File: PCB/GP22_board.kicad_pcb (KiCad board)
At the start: 4 copper layers, 100 x 100 mm, 146 parts, among them CON1 5V power input, IC1 ATMEGA328P-A, P1 TTLOut1, P10 S- DC/AC, P11 S+ DC/AC, P12 S- DC/AC, P13 TTLOut2, P14 TTLOut3, P15 PWR_SEL, P16 FILT_SEL, P2 SineInput, P3 TTLInput, P4 USB_OTG, P5 ICSP, P6 STInput, P7 S+ DC/AC, P8 S- DC/AC, P9 S+ DC/AC, SW1 START, SW2 STOP1, SW3 STOP2, U1 RS 252-210, U10 XC6206, U11 ISO7242, U12 FT232RL, U2 GP22, U3 LTC6957-4, U4 ISO3088, U5 IDT49FCT, U6 LD1117S33TR, U7 MC74VHC1GT04, U8 SN74LV8154, U9 SC74HC165N, X1 TSX-3225 X1E0000210013, Y1 4MHz, Y2 32.768 kHz

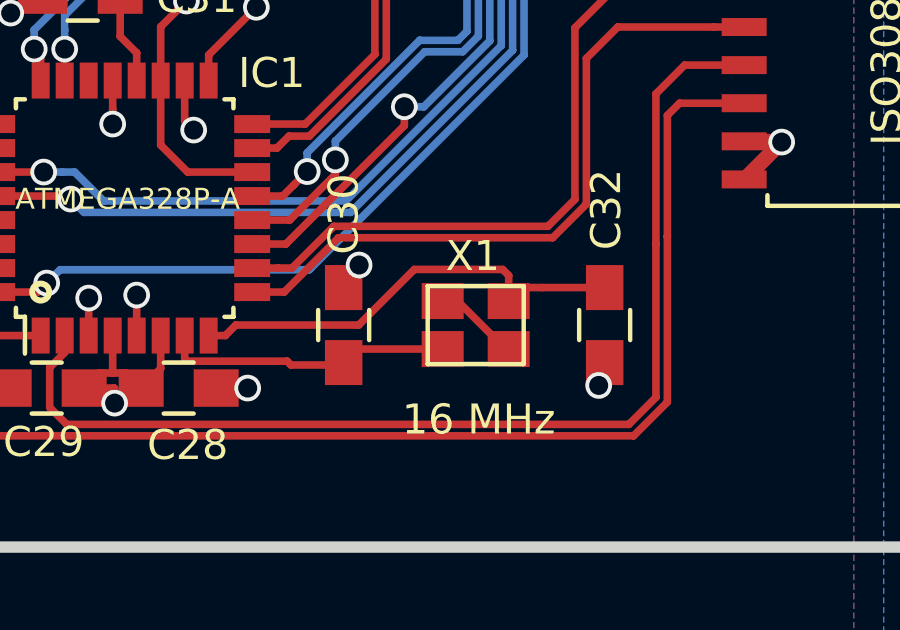
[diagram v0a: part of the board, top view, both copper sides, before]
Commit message: Create netlist and update board: no changes except to crystal grounding
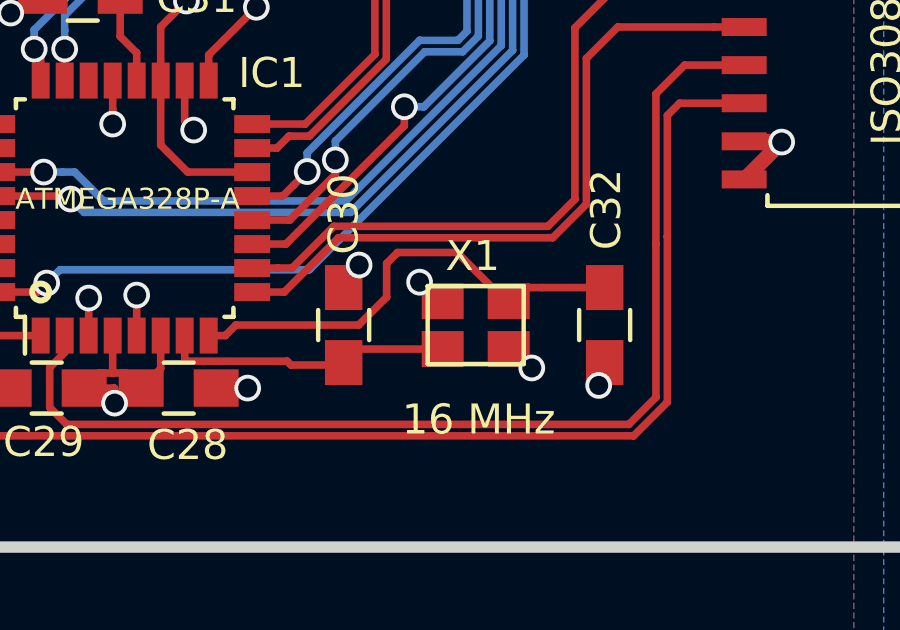
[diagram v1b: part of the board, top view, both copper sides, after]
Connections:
- D1 pad 1: (no net) -> Net-(D1-Pad1)
- D1 pad 5: (no net) -> Net-(D1-Pad5)
- D6 pad 1: (no net) -> Net-(D6-Pad1)
- D6 pad 5: (no net) -> Net-(D6-Pad5)
- D7 pad 1: (no net) -> Net-(D7-Pad1)
- D7 pad 5: (no net) -> Net-(D7-Pad5)
- IC1 pad 22: (no net) -> /DIYino/A7_inputonly
- JP1 pad 1: (no net) -> Net-(JP1-Pad1)
- P4 pad 4: (no net) -> Net-(P4-Pad4)
- SW1 pad 2a: (no net) -> Net-(SW1-Pad2a)
- SW1 pad 3a: (no net) -> Net-(SW1-Pad3a)
- SW1 pad 3b: (no net) -> Net-(SW1-Pad3b)
- SW2 pad 2a: (no net) -> Net-(SW2-Pad2a)
- SW2 pad 3a: (no net) -> Net-(SW2-Pad3a)
- SW2 pad 3b: (no net) -> Net-(SW2-Pad3b)
- SW3 pad 2a: (no net) -> Net-(SW3-Pad2a)
- SW3 pad 3a: (no net) -> Net-(SW3-Pad3a)
- SW3 pad 3b: (no net) -> Net-(SW3-Pad3b)
- U1 pad A17: (no net) -> Net-(U1-PadA17)
- U1 pad A18: (no net) -> Net-(U1-PadA18)
- U1 pad A19: (no net) -> Net-(U1-PadA19)
- U1 pad A20: (no net) -> Net-(U1-PadA20)
- U1 pad A21: (no net) -> /BPSubsheet/21A
- U1 pad A22: (no net) -> /BPSubsheet/22A
- U1 pad A23: (no net) -> /BPSubsheet/23A
- U1 pad A24: (no net) -> /BPSubsheet/24A
- U1 pad A25: (no net) -> /BPSubsheet/25A
- U1 pad A26: (no net) -> /BPSubsheet/26A
- U1 pad A27: (no net) -> /BPSubsheet/27A
- U1 pad A28: (no net) -> /BPSubsheet/28A
- U1 pad A29: (no net) -> /BPSubsheet/29A
- U1 pad A30: (no net) -> /BPSubsheet/30A
- U1 pad B17: (no net) -> Net-(U1-PadB17)
- U1 pad B18: (no net) -> Net-(U1-PadB18)
- U1 pad B19: (no net) -> Net-(U1-PadB19)
- U1 pad B20: (no net) -> Net-(U1-PadB20)
- U1 pad B21: (no net) -> /BPSubsheet/21B
- U1 pad B22: (no net) -> /BPSubsheet/22B
- U1 pad B23: (no net) -> /BPSubsheet/23B
- U1 pad B24: (no net) -> /BPSubsheet/24B
- U1 pad B25: (no net) -> /BPSubsheet/25B
- U1 pad B26: (no net) -> /BPSubsheet/26B
- U1 pad B27: (no net) -> /BPSubsheet/27B
- U1 pad B28: (no net) -> /BPSubsheet/28B
- U1 pad B29: (no net) -> /BPSubsheet/29B
- U1 pad B30: (no net) -> /BPSubsheet/30B
- U1 pad C17: (no net) -> Net-(U1-PadC17)
- U1 pad C18: (no net) -> Net-(U1-PadC18)
- U1 pad C19: (no net) -> Net-(U1-PadC19)
- U1 pad C20: (no net) -> Net-(U1-PadC20)
- U1 pad C21: (no net) -> /BPSubsheet/21C
- U1 pad C22: (no net) -> /BPSubsheet/22C
- U1 pad C23: (no net) -> /BPSubsheet/23C
- U1 pad C24: (no net) -> /BPSubsheet/24C
- U1 pad C25: (no net) -> /BPSubsheet/25C
- U1 pad C26: (no net) -> /BPSubsheet/26C
- U1 pad C27: (no net) -> /BPSubsheet/27C
- U1 pad C28: (no net) -> /BPSubsheet/28C
- U1 pad C29: (no net) -> /BPSubsheet/29C
- U1 pad C30: (no net) -> /BPSubsheet/30C
- U11 pad 10: (no net) -> Net-(U11-Pad10)
- U11 pad 11: (no net) -> Net-(U11-Pad11)
- U11 pad 6: (no net) -> /DIYino/ISO_OUTPUT
- U11 pad 7: (no net) -> Net-(U11-Pad7)
- U12 pad 10: (no net) -> Net-(U12-Pad10)
- U12 pad 11: (no net) -> Net-(U12-Pad11)
- U12 pad 12: (no net) -> Net-(U12-Pad12)
- U12 pad 13: (no net) -> Net-(U12-Pad13)
- U12 pad 14: (no net) -> Net-(U12-Pad14)
- U12 pad 19: (no net) -> Net-(U12-Pad19)
- U12 pad 24: (no net) -> Net-(U12-Pad24)
- U12 pad 27: (no net) -> Net-(U12-Pad27)
- U12 pad 28: (no net) -> Net-(U12-Pad28)
- U12 pad 3: (no net) -> Net-(U12-Pad3)
- U12 pad 6: (no net) -> Net-(U12-Pad6)
- U12 pad 8: (no net) -> Net-(U12-Pad8)
- U12 pad 9: (no net) -> Net-(U12-Pad9)
- U2 pad 17: (no net) -> Net-(U2-Pad17)
- U2 pad 18: (no net) -> Net-(U2-Pad18)
- U2 pad 19: (no net) -> Net-(U2-Pad19)
- U2 pad 20: (no net) -> Net-(U2-Pad20)
- U2 pad 23: (no net) -> Net-(U2-Pad23)
- U2 pad 24: (no net) -> Net-(U2-Pad24)
- U2 pad 5: (no net) -> /GP22_FIRE_UP
- U2 pad 6: (no net) -> /GP22_FIRE_DOWN
- U2 pad 7: (no net) -> /GP22_FIRE_IN
- U3 pad 10: (no net) -> Net-(U3-Pad10)
- U4 pad 11: (no net) -> Net-(U4-Pad11)
- U4 pad 14: (no net) -> Net-(U4-Pad14)
- U5 pad 11: (no net) -> Net-(U5-Pad11)
- U5 pad 13: (no net) -> Net-(U5-Pad13)
- U5 pad 14: (no net) -> Net-(U5-Pad14)
- U5 pad 15: (no net) -> Net-(U5-Pad15)
- U5 pad 17: (no net) -> Net-(U5-Pad17)
- U5 pad 18: (no net) -> Net-(U5-Pad18)
- U5 pad 19: (no net) -> Net-(U5-Pad19)
- U8 pad 8: (no net) -> Net-(U8-Pad8)
- U9 pad 7: (no net) -> Net-(U9-Pad7)
- X1 pad 3: Net-(X1-Pad3) -> GND
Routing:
- net GND: track 132.8 -> 135.7 mm, vias 60 -> 62
- net Net-(X1-Pad3): track 2.86 -> 0.00 mm
- net Net-(C32-Pad1): track 15.5 -> 16.1 mm

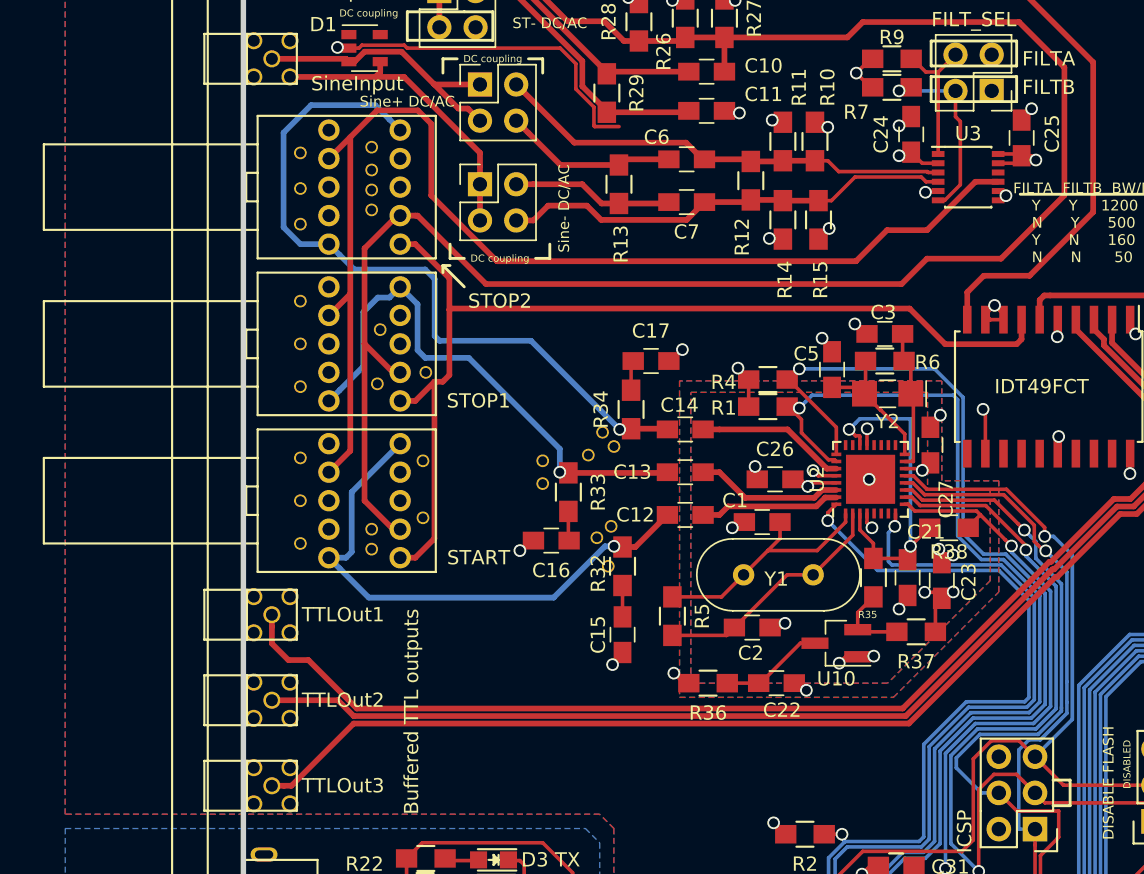
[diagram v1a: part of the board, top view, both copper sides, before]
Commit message: Fix Rotary switch footprint (NEVER TRUST KICAD FOOTPRINTS!!!)
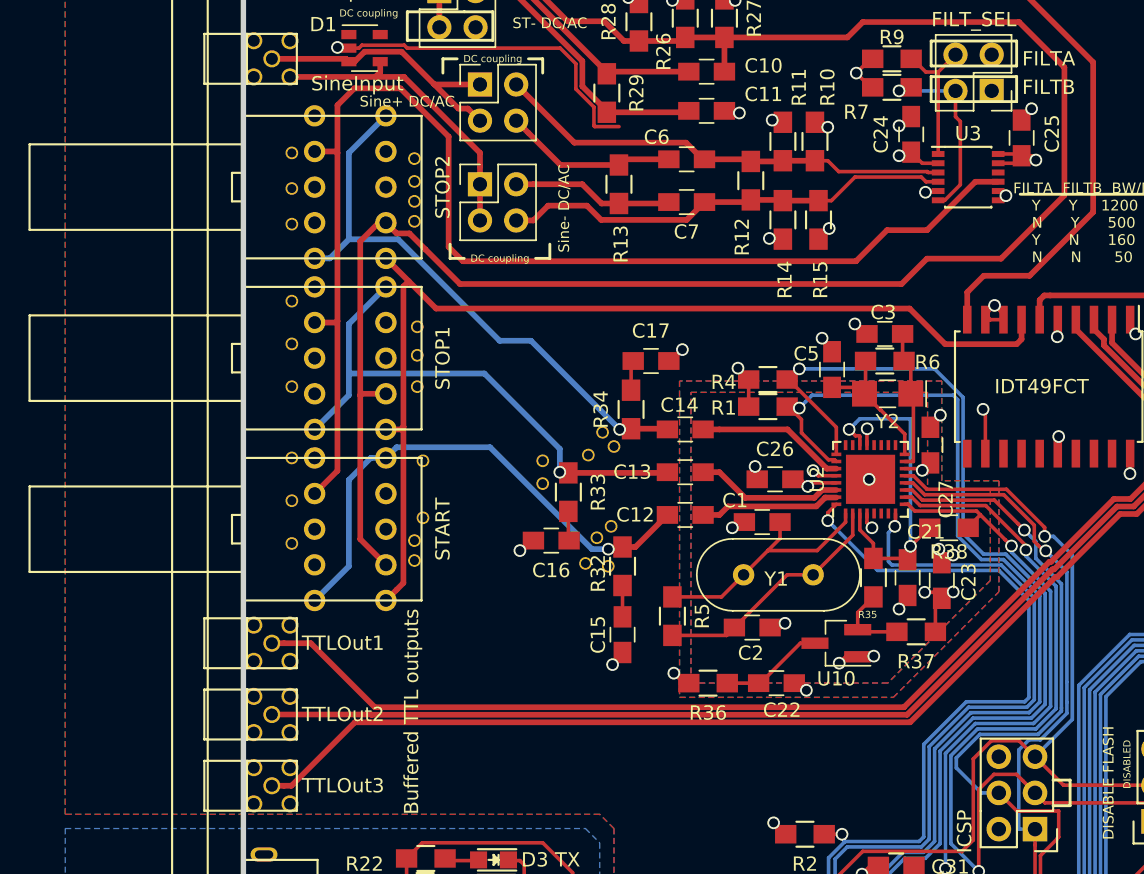
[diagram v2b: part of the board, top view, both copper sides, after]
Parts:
- added VIA**: ViaHack, Custom:ViaHack, F.Cu at (189.0, 95.4)
- SW1, SW2, SW3: footprint Custom:SP3T_switch -> Custom:ALPS_Rotary_SRBM
- moved SW1 11.2 mm to (165.0, 93.0)
- moved SW2 11.0 mm to (165.0, 81.0)
- moved SW3 11.0 mm to (165.0, 69.0)
- moved VIA** 3.10 mm to (177.0, 71.4)
- moved VIA** 3.10 mm to (177.0, 70.0)
- moved VIA** 3.10 mm to (177.0, 68.6)
- moved VIA** 3.10 mm to (177.0, 67.0)
- moved VIA** 3.10 mm to (177.0, 93.8)
- moved VIA** 3.10 mm to (177.0, 95.2)
- moved VIA** 2.81 mm to (177.2, 83.0)
- moved VIA** 2.61 mm to (177.2, 78.8)
- moved P1 2.00 mm to (167.0, 101.0)
- moved VIA** 1.34 mm to (177.2, 80.8)
- moved P13 1.00 mm to (167.0, 106.0)
- moved VIA** 0.60 mm to (168.4, 88.0)
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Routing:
- net /GP22_STOP2: track 51.5 -> 40.6 mm
- net /SineRectified: track 84.2 -> 89.9 mm
- net /TTLBufferedOut1: track 85.4 -> 83.3 mm
- net /GP22_START: track 38.1 -> 36.7 mm
- net /TTLBuffered: track 72.1 -> 73.0 mm
- net /GP22_STOP1: track 37.6 -> 38.3 mm

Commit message: Produce BOM with "Boms away"
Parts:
- removed JP1: DISABLE FLASH, Pin_Headers:Pin_Header_Straight_1x03
- removed P5: ICSP, Pin_Headers:Pin_Header_Straight_2x03
- added DISABLE_FLASH1: JMP, Pin_Headers:Pin_Header_Straight_1x03_Pitch2.54mm, F.Cu at (229.0, 113.5)
- added ICSP1: HEADER, Pin_Headers:Pin_Header_Straight_2x03_Pitch2.54mm, F.Cu at (220.5, 114.0)
- D1: footprint TO_SOT_Packages_SMD:SOT-23-5 -> TO_SOT_Packages_SMD:SOT-23-5_HandSoldering
- FILT_SEL1: renamed from P16; value FILT_SEL -> HEADER
- P10, P12, P8: value S- DC/AC -> HEADER
- P11, P7, P9: value S+ DC/AC -> HEADER
- POWER1: renamed from D2; value POWER -> LED
- POWER_SEL1: renamed from P15; value PWR_SEL -> JMP
- R12, R13, R18, R19, R28, R29: value R -> 50
- RX1: renamed from D4; value RX -> LED
- SCLK1: renamed from D5; value SCLK -> LED
- START1: renamed from SW1; value START -> DP3T
- STInput1: renamed from P6; value STInput -> MMCX
- STOP1: renamed from SW2; value STOP1 -> DP3T
- STOP2: renamed from SW3; value STOP2 -> DP3T
- SineInput1: renamed from P2; value SineInput -> MMCX
- TTLInput1: renamed from P3; value TTLInput -> MMCX
- TTLOut1: renamed from P1; value TTLOut1 -> MMCX
- TTLOut2: renamed from P13; value TTLOut2 -> MMCX
- TTLOut3: renamed from P14; value TTLOut3 -> MMCX
- TX1: renamed from D3; value TX -> LED
- U1: value RS 252-210 -> Right Angle
- U7: value MC74VHC1GT04 -> MC74VHC1G04DTT1G
- X1: value TSX-3225 X1E0000210013 -> TSX-3225 X1E0000210013

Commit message: Labelling tweaks
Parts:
- R12, R13, R18, R19, R28, R29: value 50 -> 50R

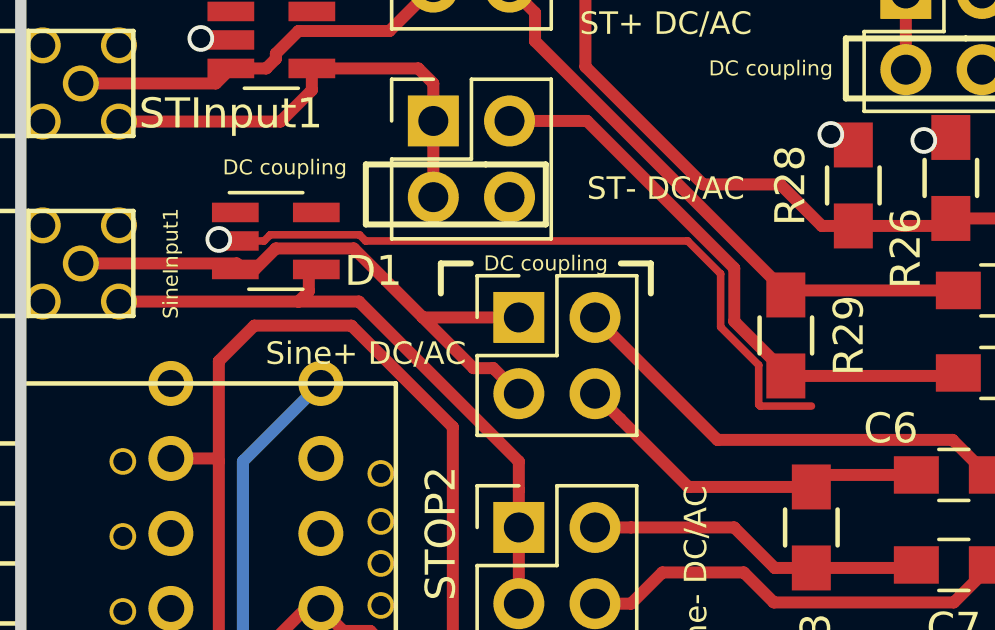
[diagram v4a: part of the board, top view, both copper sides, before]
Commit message: Remove redundant trace spottted by Newbury
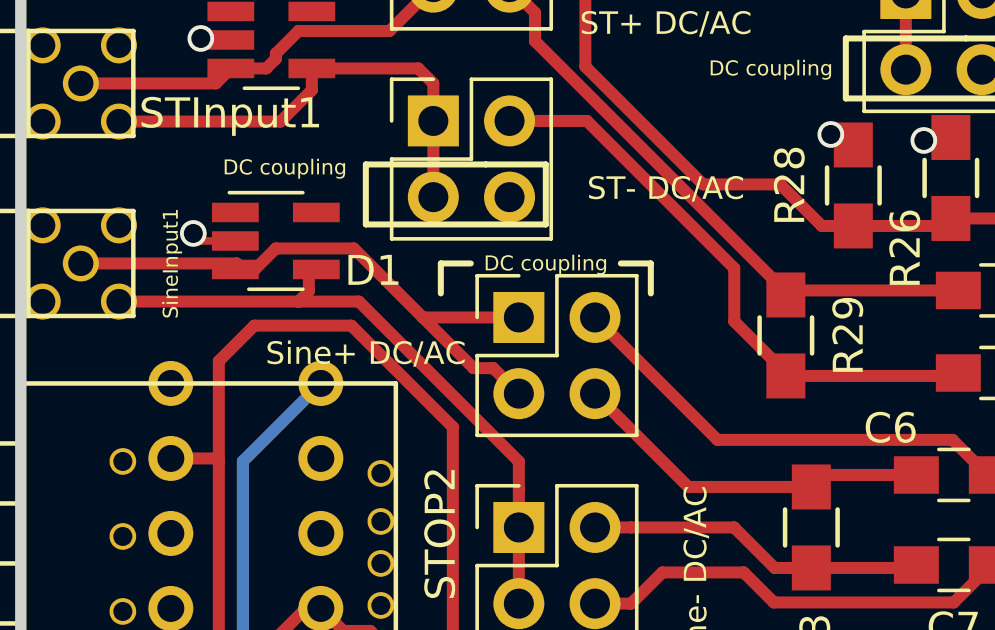
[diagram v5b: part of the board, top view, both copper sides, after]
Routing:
- net GND: track 135.7 -> 114.0 mm
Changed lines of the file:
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@@
     (links 406)
     (no_connects 14)
-    (area 24.5 19.5 276.000001 160.625)
+    (area 0 0 0 0)
     (thickness 1.6)
     (drawings 78)
-    (tracks 1408)
+    (tracks 1399)
     (zones 0)
     (modules 147)
@@
     (1 In1.Cu signal hide)
     (2 In2.Cu signal hide)
-    (31 B.Cu signal)
+    (31 B.Cu signal hide)
     (32 B.Adhes user)
     (33 F.Adhes user)
@@
   (segment (start 241.7 115.125) (end 242.15 115.125) (width 0.254) (layer F.Cu) (net 24))
   (segment (start 242.125 115.1) (end 242.15 115.125) (width 0.254) (layer F.Cu) (net 24))
+  (segment (start 172.15 59.25) (end 171 59.25) (width 0.254) (layer F.Cu) (net 25))
+  (via (at 170.75 59) (size 0.889) (drill 0.635) (layers F.Cu B.Cu) (net 25))
+  (segment (start 171 59.25) (end 170.75 59) (width 0.254) (layer F.Cu) (net 25))
   (segment (start 165.73 102.27) (end 165.73 101.421472) (width 0.254) (layer In1.Cu) (net 25))
   (segment (start 165.73 101.421472) (end 165.73 99.73) (width 0.254) (layer In1.Cu) (net 25))
@@
   (segment (start 212.937425 69.275) (end 212.851007 69.361418) (width 0.254) (layer F.Cu) (net 25))
   (via (at 212.851007 69.361418) (size 0.889) (drill 0.635) (layers F.Cu B.Cu) (net 25))
-  (segment (start 172.4 59.25) (end 173.107933 59.25) (width 0.254) (layer F.Cu) (net 25))
-  (segment (start 173.107933 59.25) (end 173.311943 59.04599) (width 0.254) (layer F.Cu) (net 25))
-  (segment (start 173.311943 59.04599) (end 176.288057 59.04599) (width 0.254) (layer F.Cu) (net 25))
-  (segment (start 176.288057 59.04599) (end 176.492067 59.25) (width 0.254) (layer F.Cu) (net 25))
-  (segment (start 176.492067 59.25) (end 187.229606 59.25) (width 0.254) (layer F.Cu) (net 25))
-  (segment (start 187.229606 59.25) (end 188.326999 60.347393) (width 0.254) (layer F.Cu) (net 25))
-  (segment (start 188.326999 60.347393) (end 188.326999 62.119066) (width 0.254) (layer F.Cu) (net 25))
-  (segment (start 188.326999 62.119066) (end 189.595999 63.388066) (width 0.254) (layer F.Cu) (net 25))
-  (segment (start 189.595999 63.388066) (end 189.595999 64.703201) (width 0.254) (layer F.Cu) (net 25))
-  (segment (start 189.595999 64.703201) (end 189.646799 64.754001) (width 0.254) (layer F.Cu) (net 25))
-  (segment (start 189.646799 64.754001) (end 191.353201 64.754001) (width 0.254) (layer F.Cu) (net 25))
   (segment (start 172.4 59.25) (end 171.65 59.25) (width 0.254) (layer F.Cu) (net 25))
   (segment (start 171.65 59.25) (end 171.6 59.2) (width 0.254) (layer F.Cu) (net 25))
-  (via (at 171.6 59.2) (size 0.889) (drill 0.635) (layers F.Cu B.Cu) (net 25))
   (segment (start 185.35 93.8) (end 185.1 93.8) (width 0.254) (layer F.Cu) (net 25))
   (segment (start 185.1 93.8) (end 184.4 94.5) (width 0.254) (layer F.Cu) (net 25))

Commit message: Get final cap values for BOM order with PCBTrain
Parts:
- C1, C2, C3, C5: value C -> 3p3
- C15, C16, C17: value 10p -> x
- R5: value R -> 1M
- R6: value R -> x
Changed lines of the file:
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@@
     (links 406)
     (no_connects 14)
-    (area 0 0 0 0)
+    (area 24.5 19.5 276.000001 160.625)
     (thickness 1.6)
     (drawings 78)
@@
       (effects (font (size 1 1) (thickness 0.15)))
     )
-    (fp_text value 10p (at 0 2.1 270) (layer F.Fab)
+    (fp_text value x (at 0 2.1 270) (layer F.Fab)
       (effects (font (size 1 1) (thickness 0.15)))
     )
@@
       (effects (font (size 1 1) (thickness 0.15)))
     )
-    (fp_text value 10p (at 0 2.1 180) (layer F.Fab)
+    (fp_text value x (at 0 2.1 180) (layer F.Fab)
       (effects (font (size 1 1) (thickness 0.15)))
     )
@@
       (effects (font (size 1 1) (thickness 0.15)))
     )
-    (fp_text value C (at 0 2.1 180) (layer F.Fab)
+    (fp_text value 3p3 (at 0 2.1 180) (layer F.Fab)
       (effects (font (size 1 1) (thickness 0.15)))
     )
@@
       (effects (font (size 1 1) (thickness 0.15)))
     )
-    (fp_text value C (at 0 2.1) (layer F.Fab)
+    (fp_text value 3p3 (at 0 2.1) (layer F.Fab)
       (effects (font (size 1 1) (thickness 0.15)))
     )
@@
       (effects (font (size 1 1) (thickness 0.15)))
     )
-    (fp_text value C (at 0 2.1 180) (layer F.Fab)
+    (fp_text value 3p3 (at 0 2.1 180) (layer F.Fab)
       (effects (font (size 1 1) (thickness 0.15)))
     )
@@
       (effects (font (size 1 1) (thickness 0.15)))
     )
-    (fp_text value C (at 0 2.1 90) (layer F.Fab)
+    (fp_text value 3p3 (at 0 2.1 90) (layer F.Fab)
       (effects (font (size 1 1) (thickness 0.15)))
     )
@@
       (effects (font (size 1 1) (thickness 0.15)))
     )
-    (fp_text value 10p (at 0 2.1) (layer F.Fab)
+    (fp_text value x (at 0 2.1) (layer F.Fab)
       (effects (font (size 1 1) (thickness 0.15)))
     )
@@
       (effects (font (size 1 1) (thickness 0.15)))
     )
-    (fp_text value R (at 0 2.1 270) (layer F.Fab)
+    (fp_text value 1M (at 0 2.1 270) (layer F.Fab)
       (effects (font (size 1 1) (thickness 0.15)))
     )
@@
       (effects (font (size 1 1) (thickness 0.15)))
     )
-    (fp_text value R (at 0 2.1) (layer F.Fab)
-      (effects (font (size 1 1) (thickness 0.15)))
-    )
+    (fp_text value x (at 0 2.1) (layer F.Fab)
+      (effects (font (size 1 1) (thickness 0.15)))
+    )
